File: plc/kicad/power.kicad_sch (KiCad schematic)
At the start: 85 parts, among them Q5 BSS138LT1G, Q6 CSD19537Q3, SW3 TSD003B08026A03, U14 LMR16006XDDCR, U15 TPS7A5201QRGRRQ1, U16 TPS26630RGER, U21 TPS54560BDDAR

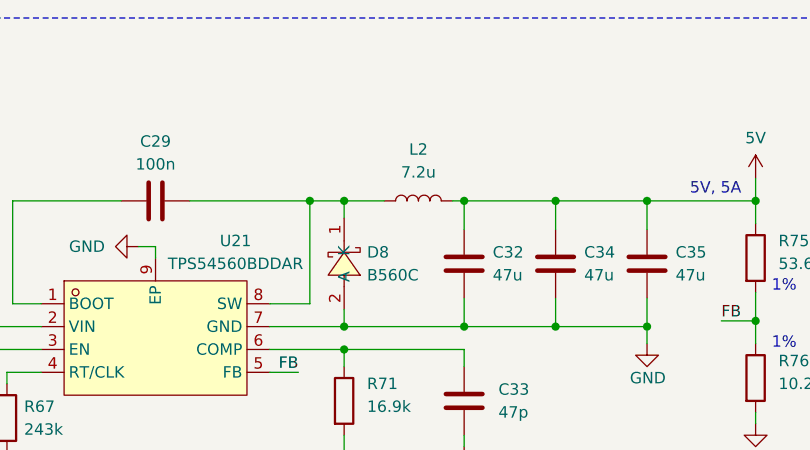
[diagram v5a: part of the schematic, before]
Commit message: Added TPS54560 PCB placement
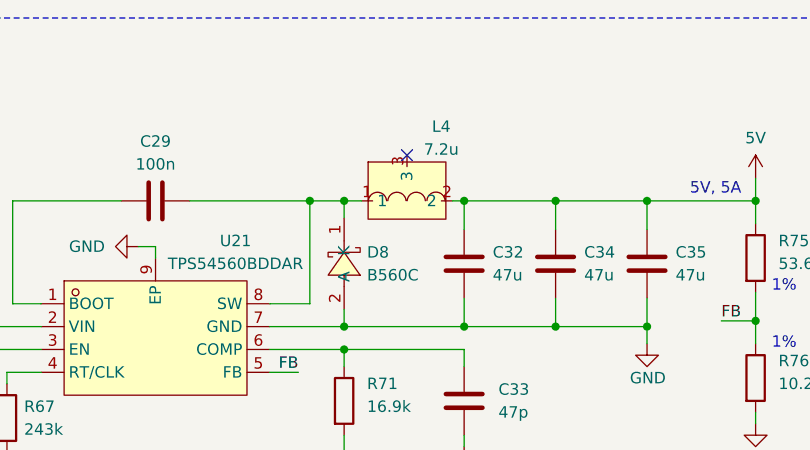
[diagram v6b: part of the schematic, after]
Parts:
- removed L2: 7.2u, Inductor_SMD:L_1206_3216Metric, symbol Device:L
- added L4: 7.2u, LibrePLC32:IND-SMD_3P-L13.5-W13.0-P6.9, symbol LibrePLC32:XRCEP125-7R2M
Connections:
- net 5V: now also L4.2
- net at C29.2, D8.1 (K), U21.8 (SW): now also L4.1
- no-connect marks 15 -> 16
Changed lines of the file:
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@@
 	)
 	(junction
+		(at 128.27 40.005)
+		(diameter 0)
+		(color 0 0 0 0)
+	)
+	(junction
 		(at 325.12 205.74)
 		(diameter 0)
@@
 	)
 	(junction
-		(at 128.27 40.005)
-		(diameter 0)
-		(color 0 0 0 0)
-	)
-	(junction
 		(at 34.29 119.38)
 		(diameter 0)
@@
 	)
 	(no_connect
+		(at 135.255 34.925)
+	)
+	(no_connect
 		(at 116.205 207.01)
 	)
@@
 	(wire
 		(pts
-			(xy 128.27 40.005) (xy 132.715 40.005)
-		)
-		(stroke
-			(width 0)
-			(type default)
-		)
-	)
-	(wire
-		(pts
 			(xy 146.05 118.11) (xy 135.89 118.11)
 		)
@@
 	(wire
 		(pts
+			(xy 128.27 40.005) (xy 130.175 40.005)
+		)
+		(stroke
+			(width 0)
+			(type default)
+		)
+	)
+	(wire
+		(pts
 			(xy 177.165 243.205) (xy 177.165 245.745)
 		)
@@
 	)
 	(symbol
+		(lib_id "LibrePLC32:XRCEP125-7R2M")
+		(at 135.255 38.735 0)
+		(unit 1)
+		(body_style 1)
+		(exclude_from_sim no)
+		(in_bom yes)
+		(on_board yes)
+		(in_pos_files yes)
+		(dnp no)
+		(property "Reference" "L4"
+			(at 139.065 31.75 0)
+			(show_name no)
+			(do_not_autoplace no)
+			(effects
+				(font
+					(size 1.27 1.27)
+				)
+			)
+		)
+		(property "Value" "7.2u"
+			(at 139.065 34.29 0)
+			(show_name no)
+			(do_not_autoplace no)
+			(effects
+				(font
+					(size 1.27 1.27)
+				)
+			)
+		)
+		(property "Footprint" "LibrePLC32:IND-SMD_3P-L13.5-W13.0-P6.9"
+			(at 135.255 47.625 0)
+			(hide yes)
+			(show_name no)
+			(do_not_autoplace no)
+			(effects
+				(font
+					(size 1.27 1.27)
+				)
+			)
+		)
+		(property "Datasheet" "https://www.lcsc.com/datasheet/C41368782.pdf"
+			(at 135.255 50.165 0)
+			(hide yes)
+			(show_name no)
+			(do_not_autoplace no)
+			(effects
+				(font
+					(size 1.27 1.27)
+				)
+			)
+		)
+		(property "Description" ""
+			(at 135.255 38.735 0)
+			(hide yes)
+			(show_name no)
+			(do_not_autoplace no)
+			(effects
+				(font
+					(size 1.27 1.27)
+				)
+			)
+		)
+		(property "Manufacturer" "XR(祥如)"
+			(at 135.255 52.705 0)
+			(hide yes)
+			(show_name no)
+			(do_not_autoplace no)
+			(effects
+				(font
+					(size 1.27 1.27)
+				)
+			)
+		)
+		(property "MPN" "XRCEP125-7R2M"
+			(at 135.255 55.245 0)
+			(hide yes)
+			(show_name no)
+			(do_not_autoplace no)
+			(effects
+				(font
+					(size 1.27 1.27)
+				)
+			)
+		)
+		(property "LCSC Part" "C41368782"
+			(at 135.255 57.785 0)
+			(hide yes)
+			(show_name no)
+			(do_not_autoplace no)
+			(effects
+				(font
+					(size 1.27 1.27)
+				)
+			)
+		)
+		(pin "3"
+		)
+		(pin "1"
+		)
+		(pin "2"
+		)
+		(instances
+			(project "LibrePLC32"
+				(path "/ef4c1a27-85a3-413a-9f93-a41c4f97eee5/7cb27fd0-1c73-4e87-ad2d-fb4e463ee9fb"
+					(reference "L4")
+					(unit 1)
+				)
+			)
+		)
+	)
+	(symbol
 		(lib_id "power:VBUS")
 		(at 368.3 114.3 180)
@@
 					(unit 1)
 				)
-			)
-		)
-	)
-	(symbol
-		(lib_id "Device:L")
-		(at 136.525 40.005 90)
-		(unit 1)
-		(body_style 1)
-		(exclude_from_sim no)
-		(in_bom yes)
-		(on_board yes)
-		(in_pos_files yes)
-		(dnp no)
-		(fields_autoplaced yes)
-		(property "Reference" "L2"
-			(at 136.525 34.29 90)
-			(show_name no)
-			(do_not_autoplace no)
-			(effects
-				(font
-					(size 1.27 1.27)
-				)
-			)
-		)
-		(property "Value" "7.2u"
-			(at 136.525 36.83 90)
-			(show_name no)
-			(do_not_autoplace no)
-			(effects
-				(font
-					(size 1.27 1.27)
-				)
-			)
-		)
-		(property "Footprint" "Inductor_SMD:L_1206_3216Metric"
-			(at 136.525 40.005 0)
-			(hide yes)
-			(show_name no)
-			(do_not_autoplace no)
-			(effects
-				(font
-					(size 1.27 1.27)
-				)
-			)
-		)
-		(property "Datasheet" ""
-			(at 136.525 40.005 0)
-			(hide yes)
-			(show_name no)
-			(do_not_autoplace no)
-			(effects
-				(font
-					(size 1.27 1.27)
-				)
-			)
-		)
-		(property "Description" "Inductor"
-			(at 136.525 40.005 0)
-			(hide yes)
-			(show_name no)
-			(do_not_autoplace no)
-			(effects
-				(font
-					(size 1.27 1.27)
-				)
-			)
-		)
-		(pin "2"
-		)
-		(pin "1"
-		)
-		(instances
-			(project "LibrePLC32"
-				(path "/ef4c1a27-85a3-413a-9f93-a41c4f97eee5/7cb27fd0-1c73-4e87-ad2d-fb4e463ee9fb"
-					(reference "L2")
-					(unit 1)
-				)

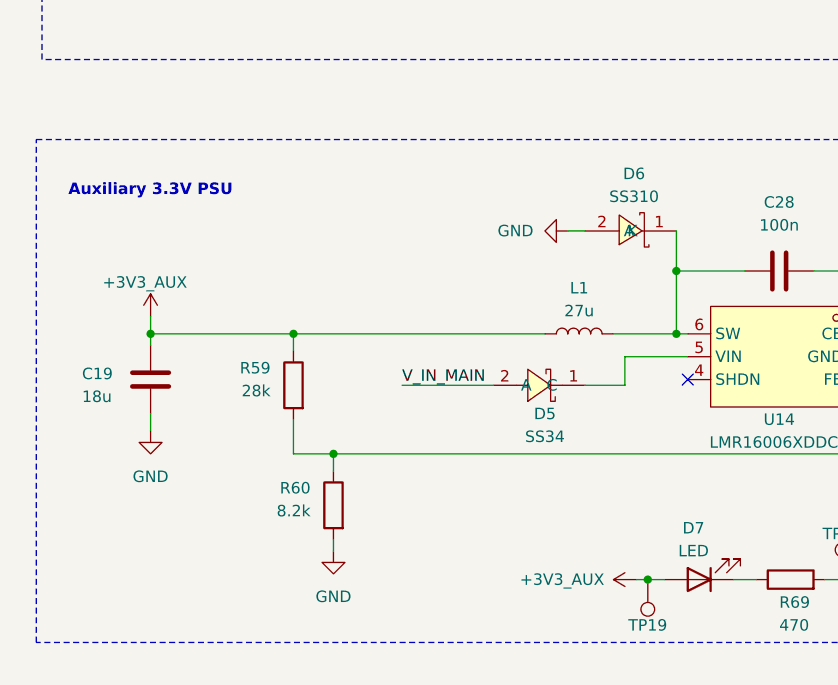
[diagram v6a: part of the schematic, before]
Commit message: LMR16006X PCB placement
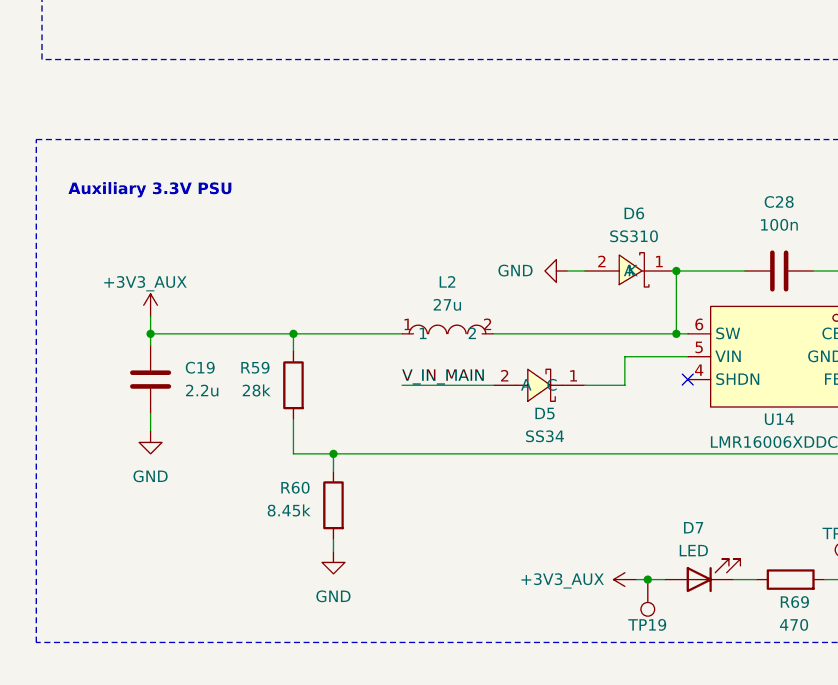
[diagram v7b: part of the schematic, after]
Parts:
- removed L1: 27u, Inductor_SMD:L_1206_3216Metric, symbol Device:L
- added L2: 27u, LibrePLC32:IND-SMD_L3.5-W3.0_SLF0302, symbol LibrePLC32:ASPI-0315S-270M-T
- C19: value 18u -> 2.2u; footprint Capacitor_SMD:C_0603_1608Metric -> Capacitor_SMD:C_1206_3216Metric
- R60: value 8.2k -> 8.45k
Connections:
- net +3V3_AUX: now also C19.1, L2.1; no longer C19.2
- net GND: now also C19.2; no longer C19.1
- net at C28.2, D6.1 (K), U14.6 (SW): now also L2.2
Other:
- moved on the sheet: D6

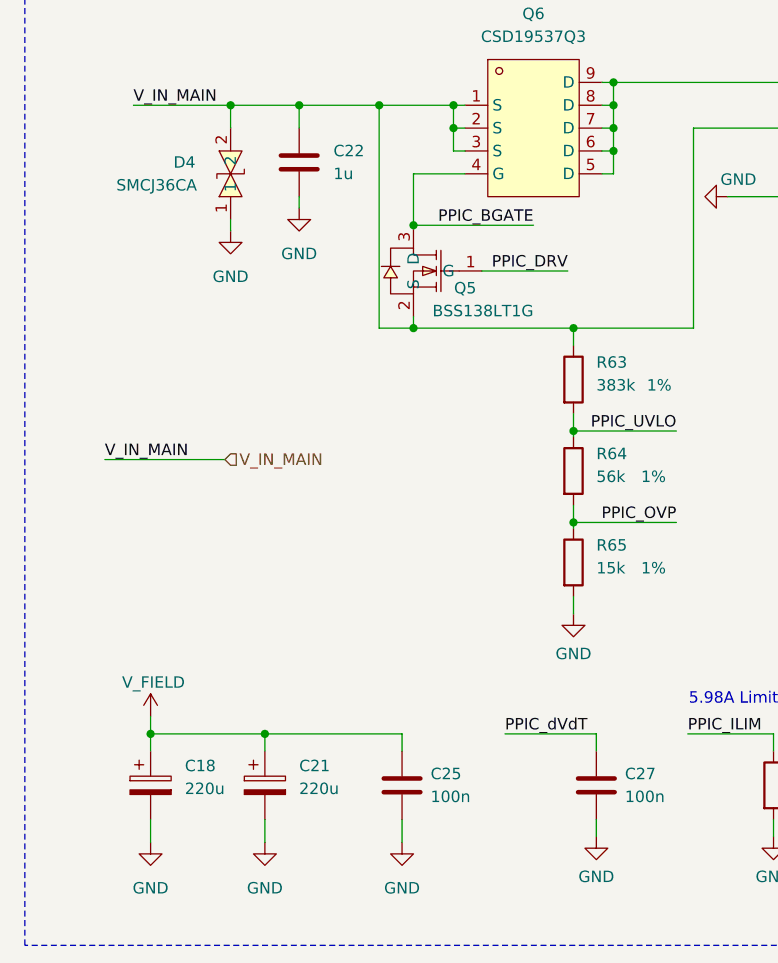
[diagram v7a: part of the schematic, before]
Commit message: TPS26630 PCB placement
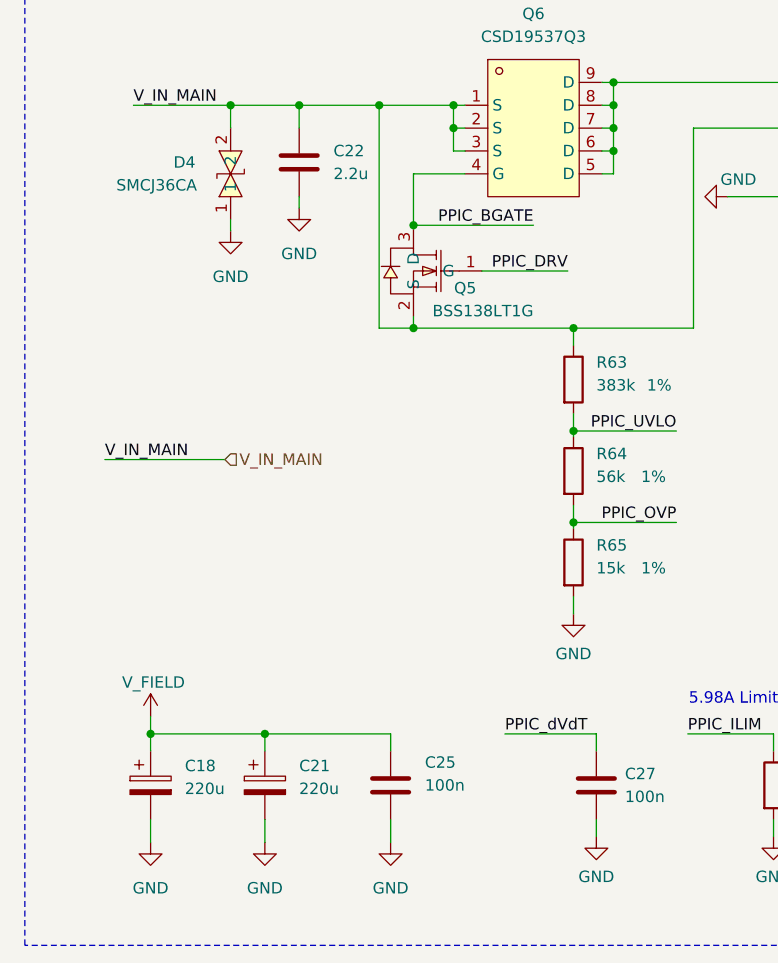
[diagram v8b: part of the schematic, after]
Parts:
- C18, C21: footprint Capacitor_SMD:C_0603_1608Metric -> Capacitor_SMD:C_Elec_10x10.2
- C22: value 1u -> 2.2u; footprint Capacitor_SMD:C_0603_1608Metric -> Capacitor_SMD:C_1206_3216Metric
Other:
- moved on the sheet: C25
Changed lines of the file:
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@@
 	(wire
 		(pts
-			(xy 46.99 254) (xy 62.23 254)
+			(xy 46.99 254) (xy 60.96 254)
 		)
 		(stroke
@@
 	(wire
 		(pts
-			(xy 62.23 266.065) (xy 62.23 263.525)
+			(xy 60.96 266.065) (xy 60.96 263.525)
 		)
 		(stroke
@@
 	(wire
 		(pts
-			(xy 62.23 254) (xy 62.23 255.905)
+			(xy 60.96 254) (xy 60.96 255.905)
 		)
 		(stroke
@@
 	(symbol
 		(lib_id "power:GND")
-		(at 62.23 266.065 0)
+		(at 60.96 266.065 0)
 		(unit 1)
 		(body_style 1)
@@
 		(fields_autoplaced yes)
 		(property "Reference" "#PWR0138"
-			(at 62.23 272.415 0)
+			(at 60.96 272.415 0)
 			(hide yes)
 			(show_name no)
@@
 		)
 		(property "Value" "GND"
-			(at 62.23 271.145 0)
+			(at 60.96 271.145 0)
 			(show_name no)
 			(do_not_autoplace no)
@@
 		)
 		(property "Footprint" ""
-			(at 62.23 266.065 0)
+			(at 60.96 266.065 0)
 			(hide yes)
 			(show_name no)
@@
 		)
 		(property "Datasheet" ""
-			(at 62.23 266.065 0)
+			(at 60.96 266.065 0)
 			(hide yes)
 			(show_name no)
@@
 		)
 		(property "Description" "Power symbol creates a global label with name \"GND\" , ground"
-			(at 62.23 266.065 0)
+			(at 60.96 266.065 0)
 			(hide yes)
 			(show_name no)
@@
 			)
 		)
-		(property "Footprint" "Capacitor_SMD:C_0603_1608Metric"
+		(property "Footprint" "Capacitor_SMD:C_Elec_10x10.2"
 			(at 35.2552 263.525 0)
 			(hide yes)
@@
 			)
 		)
-		(property "Footprint" "Capacitor_SMD:C_0603_1608Metric"
+		(property "Footprint" "Capacitor_SMD:C_Elec_10x10.2"
 			(at 47.9552 263.525 0)
 			(hide yes)
@@
 			)
 		)
-		(property "Value" "1u"
+		(property "Value" "2.2u"
 			(at 54.61 191.7699 0)
 			(show_name no)
@@
 			)
 		)
-		(property "Footprint" "Capacitor_SMD:C_0603_1608Metric"
+		(property "Footprint" "Capacitor_SMD:C_1206_3216Metric"
 			(at 49.8348 186.69 0)
 			(hide yes)
@@
 	(symbol
 		(lib_id "Device:C")
-		(at 62.23 259.715 180)
+		(at 60.96 259.715 180)
 		(unit 1)
 		(body_style 1)
@@
 		(in_pos_files yes)
 		(dnp no)
-		(fields_autoplaced yes)
 		(property "Reference" "C25"
-			(at 65.405 258.4449 0)
+			(at 64.77 257.175 0)
 			(show_name no)
 			(do_not_autoplace no)
@@
 		)
 		(property "Value" "100n"
-			(at 65.405 260.9849 0)
+			(at 64.77 259.715 0)
 			(show_name no)
 			(do_not_autoplace no)
@@
 		)
 		(property "Footprint" "Capacitor_SMD:C_0603_1608Metric"
-			(at 61.2648 255.905 0)
+			(at 59.9948 255.905 0)
 			(hide yes)
 			(show_name no)
@@
 		)
 		(property "Datasheet" ""
-			(at 62.23 259.715 0)
+			(at 60.96 259.715 0)
 			(hide yes)
 			(show_name no)
@@
 		)
 		(property "Description" "Unpolarized capacitor"
-			(at 62.23 259.715 0)
+			(at 60.96 259.715 0)
 			(hide yes)
 			(show_name no)
